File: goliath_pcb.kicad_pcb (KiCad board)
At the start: 2 copper layers, 138.4 x 81.9 mm, 56 parts, among them IC1 MCT9001SD, IC2 MCT9001SD, IC3 MCT9001SD, IC4 MCT9001SD, IC5 MCT9001SD, IC6 MCT9001SD, IC7 MCT9001SD, J1 RJ45_LED, J2 RJ45_LED, J3 RJ45_LED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

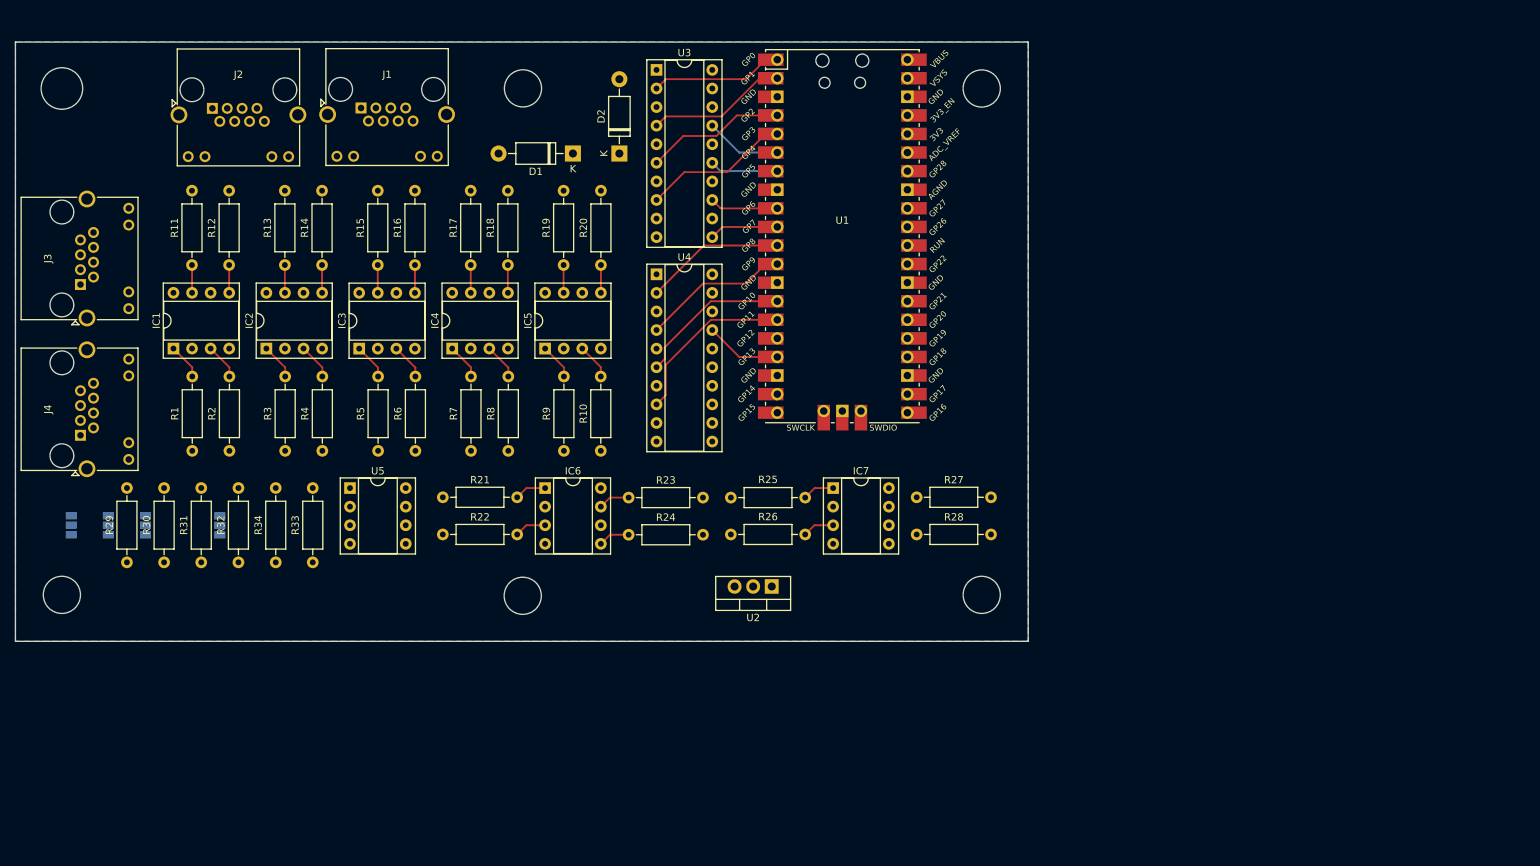
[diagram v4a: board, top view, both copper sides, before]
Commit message: Add xBee initial plan
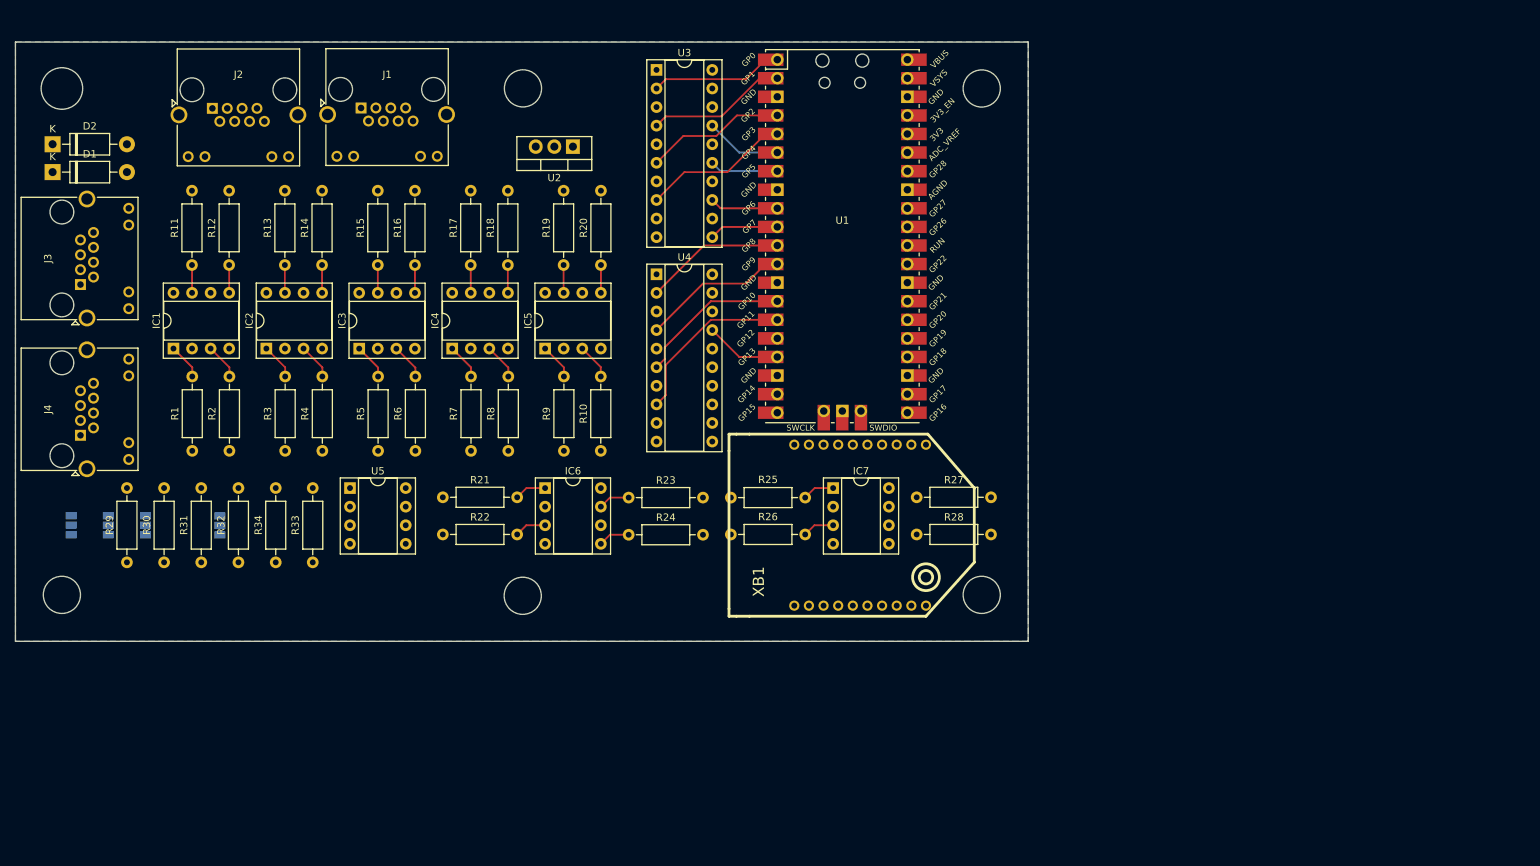
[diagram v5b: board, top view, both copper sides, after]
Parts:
- added XB1: XBEE, RF_and_other_modules:XBEE_PRO_PTH, F.Cu at (160.0, 113.0)
- moved D2 77.5 mm to (40.6, 61.0), turned to 0 degrees
- moved D1 71.2 mm to (40.6, 64.8), turned to 0 degrees
- moved U2 66.0 mm to (111.8, 61.3)
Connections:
- U1 pad 21: Net-(J4-Pad3) -> Net-(U1-Pad21)
- U1 pad 22: Net-(J4-Pad4) -> Net-(U1-Pad22)
- U1 pad 24: unconnected-(U1-Pad24) -> Net-(J4-Pad3)
- U1 pad 25: unconnected-(U1-Pad25) -> Net-(J4-Pad4)

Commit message: Run traces for current version
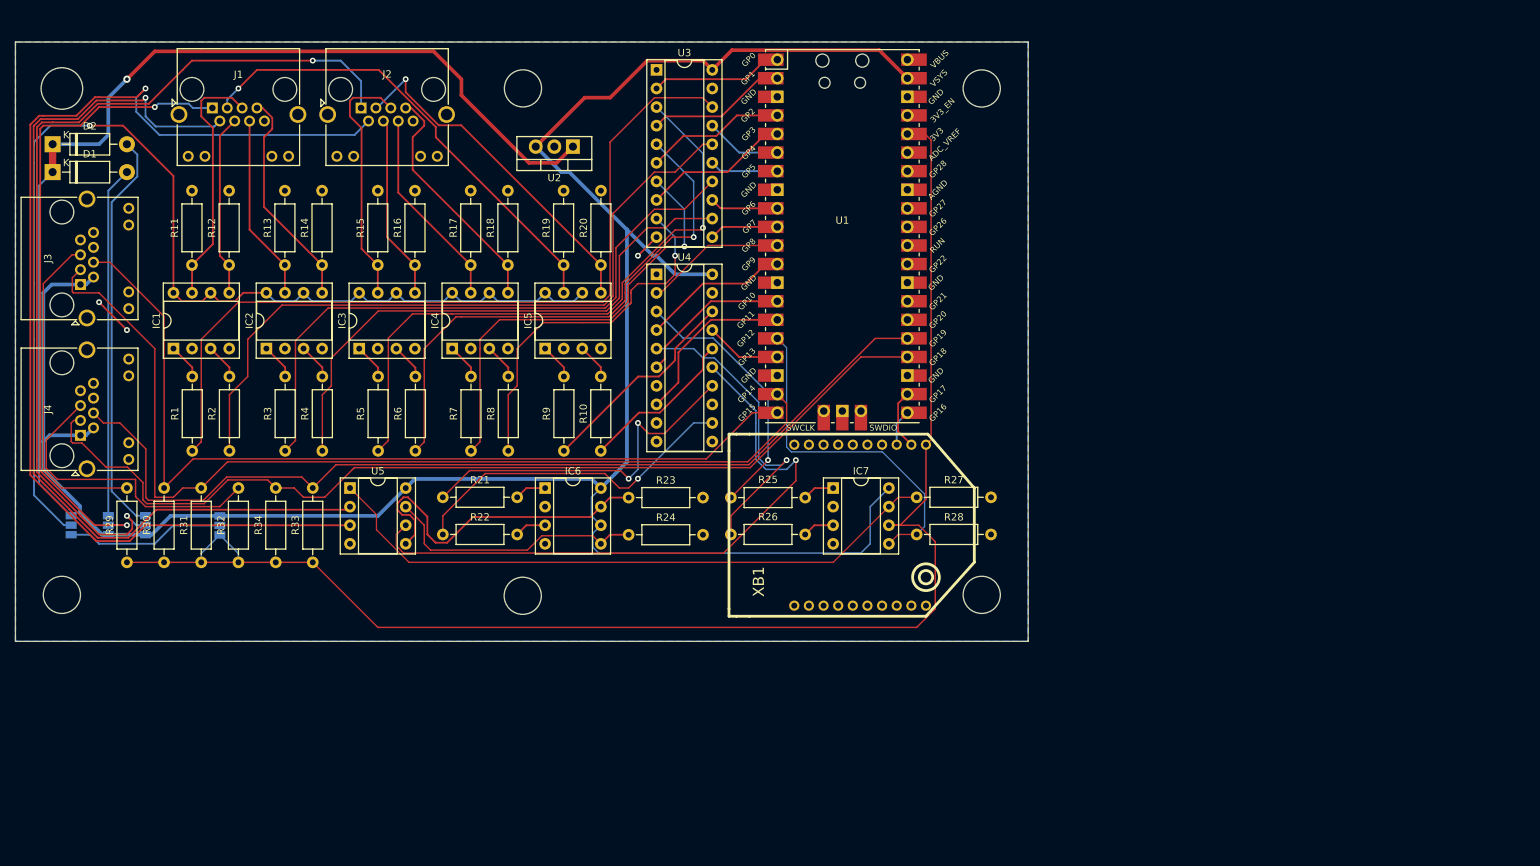
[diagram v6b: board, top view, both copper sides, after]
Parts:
- moved J2 20.3 mm to (82.8, 56.0)
- moved J1 20.3 mm to (62.5, 56.0)
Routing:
- net 5V: track 0.00 -> 307.7 mm
- net 3.3V: track 0.00 -> 200.8 mm
- net LGV: track 0.00 -> 158.1 mm, vias 0 -> 1
- net Net-(J2-Pad2): track 0.00 -> 151.6 mm, vias 0 -> 1
- net 12V: track 0.00 -> 141.2 mm, vias 0 -> 1
- net Net-(J4-Pad3): track 0.00 -> 133.4 mm
- net Net-(J3-Pad3): track 0.00 -> 133.3 mm
- net Net-(J4-Pad4): track 0.00 -> 130.5 mm
- net Net-(J1-Pad2): track 0.00 -> 126.6 mm, vias 0 -> 1
- net Net-(J3-Pad4): track 0.00 -> 124.3 mm
- net Net-(J2-Pad1): track 0.00 -> 122.1 mm, vias 0 -> 2
- net Net-(R1-Pad1): track 0.00 -> 112.0 mm
- net Net-(R2-Pad1): track 0.00 -> 97.4 mm
- net Net-(J1-Pad1): track 0.00 -> 89.4 mm, vias 0 -> 2
- net Net-(U4-Pad15): track 0.00 -> 86.9 mm, vias 0 -> 1
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
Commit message: Add extra I/O and extra headers, expand PCB
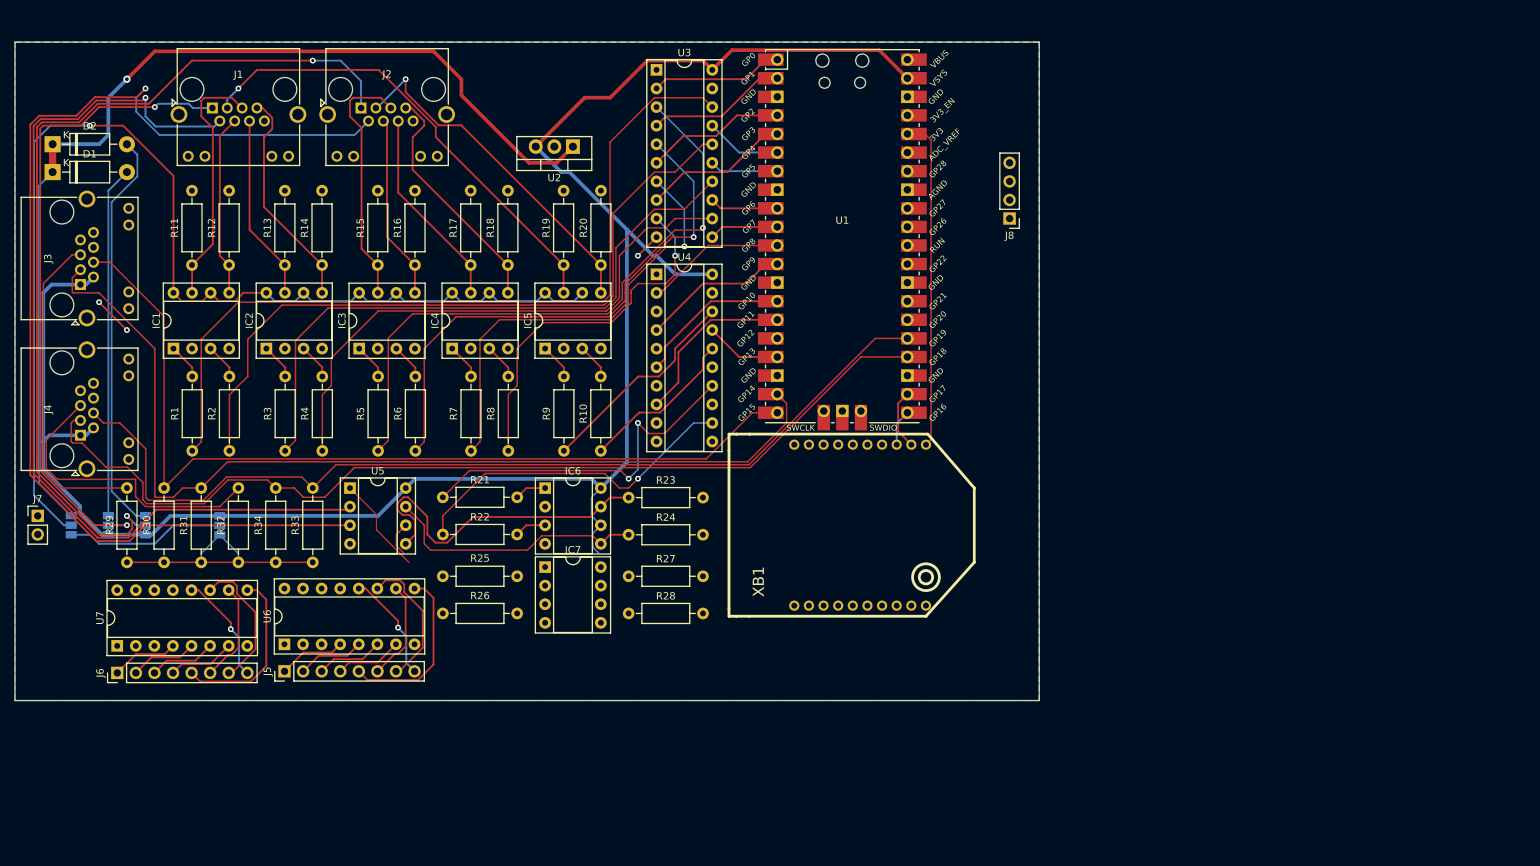
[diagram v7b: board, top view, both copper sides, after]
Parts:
- added J5: Conn_01x08_Male, Connector_PinHeader_2.54mm:PinHeader_1x08_P2.54mm_Vertical, F.Cu at (72.3, 133.0)
- added J6: Conn_01x08_Male, Connector_PinHeader_2.54mm:PinHeader_1x08_P2.54mm_Vertical, F.Cu at (49.5, 133.2)
- added J7: Conn_01x02_Male, Connector_PinHeader_2.54mm:PinHeader_1x02_P2.54mm_Vertical, F.Cu at (38.6, 111.8)
- added J8: Conn_01x04_Male, Connector_PinHeader_2.54mm:PinHeader_1x04_P2.54mm_Vertical, F.Cu at (171.4, 71.1)
- added U6: PCF8574, Package_DIP:DIP-16_W7.62mm_Socket, F.Cu at (72.3, 129.3)
- added U7: PCF8574, Package_DIP:DIP-16_W7.62mm_Socket, F.Cu at (49.5, 129.5)
- moved IC7 40.8 mm to (108.0, 118.8)
- moved R27 40.8 mm to (119.4, 120.0)
- moved R28 40.8 mm to (119.4, 125.1)
- moved R26 40.8 mm to (94.0, 125.1)
- moved R25 40.8 mm to (104.1, 120.0)
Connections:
- U1 pad 16: Net-(IC7-Pad5) -> Net-(U1-Pad16)
- U1 pad 17: Net-(U1-Pad17) -> Net-(IC7-Pad5)
- U1 pad 26: unconnected-(U1-Pad26) -> Net-(U1-Pad26)
- U1 pad 27: unconnected-(U1-Pad27) -> Net-(U1-Pad27)
- U1 pad 29: unconnected-(U1-Pad29) -> Net-(J8-Pad1)
- U1 pad 31: unconnected-(U1-Pad31) -> Net-(J8-Pad2)
- U1 pad 32: unconnected-(U1-Pad32) -> Net-(J8-Pad3)
- U1 pad 34: unconnected-(U1-Pad34) -> Net-(J8-Pad4)
- U4 pad 17: Net-(U1-Pad17) -> Net-(U1-Pad16)
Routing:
- net 3.3V: track 200.8 -> 80.5 mm
- net Net-(U4-Pad15): track 86.9 -> 4.74 mm, vias 1 -> 0
- net Net-(IC7-Pad7): track 86.6 -> 13.5 mm
- net 5V: track 307.7 -> 261.4 mm
- net Net-(R26-Pad1): track 42.5 -> 0.00 mm, vias 1 -> 0
- net Net-(IC7-Pad5): track 47.2 -> 10.4 mm
- net Net-(R25-Pad2): track 36.3 -> 0.00 mm, vias 1 -> 0
- net Net-(J5-Pad5): track 0.00 -> 23.8 mm
- net Net-(J6-Pad5): track 0.00 -> 23.8 mm
- net Net-(J5-Pad7): track 0.00 -> 19.1 mm
- net Net-(J6-Pad7): track 0.00 -> 19.1 mm
- net Net-(J6-Pad8): track 0.00 -> 15.0 mm, vias 0 -> 1
- net Net-(J5-Pad8): track 0.00 -> 15.0 mm, vias 0 -> 1
- net Net-(J6-Pad6): track 0.00 -> 13.7 mm
- net Net-(J5-Pad6): track 0.00 -> 13.7 mm
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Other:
- board size 138.4 x 81.9 mm -> 140 x 90 mm

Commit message: Add more resistors, caps
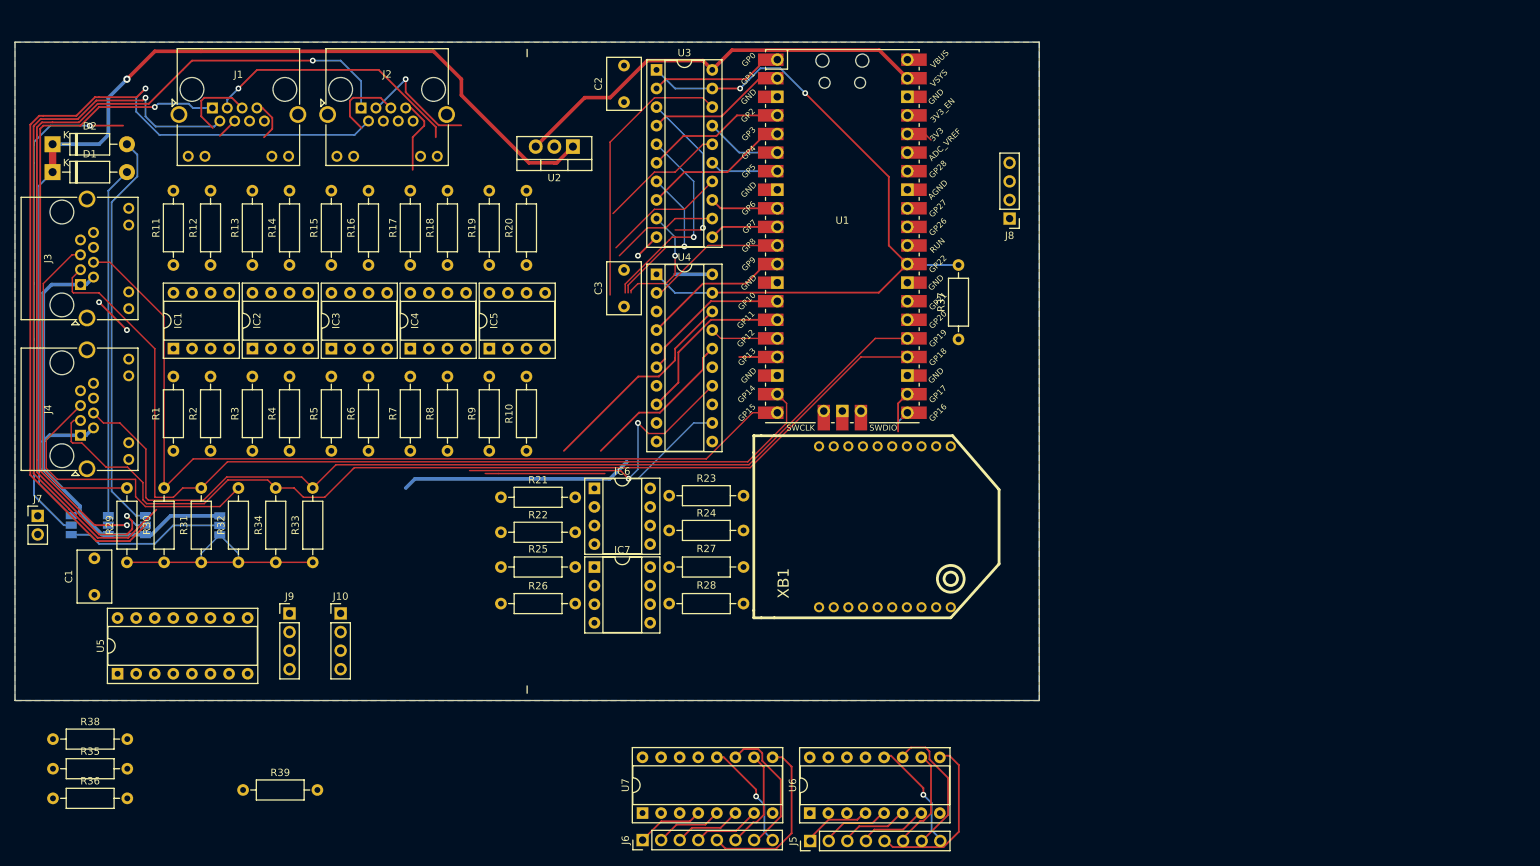
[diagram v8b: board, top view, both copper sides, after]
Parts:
- added C1: 1uF, Capacitor_THT:C_Rect_L7.0mm_W4.5mm_P5.00mm, F.Cu at (46.4, 122.6)
- added C2: 1uF, Capacitor_THT:C_Rect_L7.0mm_W4.5mm_P5.00mm, F.Cu at (118.7, 55.2)
- added C3: 1uF, Capacitor_THT:C_Rect_L7.0mm_W4.5mm_P5.00mm, F.Cu at (118.7, 83.1)
- added J10: Conn_01x04_Male, Connector_PinHeader_2.54mm:PinHeader_1x04_P2.54mm_Vertical, F.Cu at (80.0, 125.1)
- added J9: Conn_01x04_Male, Connector_PinHeader_2.54mm:PinHeader_1x04_P2.54mm_Vertical, F.Cu at (73.0, 125.1)
- added R35: 10k, Resistor_THT:R_Axial_DIN0207_L6.3mm_D2.5mm_P10.16mm_Horizontal, F.Cu at (40.7, 146.3)
- added R36: 10k, Resistor_THT:R_Axial_DIN0207_L6.3mm_D2.5mm_P10.16mm_Horizontal, F.Cu at (40.7, 150.4)
- added R37: 10k, Resistor_THT:R_Axial_DIN0207_L6.3mm_D2.5mm_P10.16mm_Horizontal, F.Cu at (164.5, 87.6)
- added R38: 10k, Resistor_THT:R_Axial_DIN0207_L6.3mm_D2.5mm_P10.16mm_Horizontal, F.Cu at (40.7, 142.3)
- added R39: 10k, Resistor_THT:R_Axial_DIN0207_L6.3mm_D2.5mm_P10.16mm_Horizontal, F.Cu at (66.7, 149.2)
- U5: value LTC1298CS8-PBF -> MCP3008; footprint Package_DIP:DIP-8_W7.62mm_Socket -> Package_DIP:DIP-16_W7.62mm_Socket
- moved J5 75.5 mm to (144.2, 156.2)
- moved U6 75.4 mm to (144.1, 152.4)
- moved U7 75.4 mm to (121.3, 152.4)
- moved J6 75.4 mm to (121.3, 156.1)
- moved U5 40.7 mm to (49.5, 133.3), turned to 90 degrees
- moved R9 10.2 mm to (100.3, 102.9)
- moved R20 10.2 mm to (105.4, 77.5)
- moved R10 10.2 mm to (105.4, 102.9)
- moved R19 10.2 mm to (100.3, 77.5)
- moved R8 8.32 mm to (94.6, 102.9)
- moved R7 8.30 mm to (89.5, 102.9)
- moved R17 8.26 mm to (89.5, 77.5)
- moved R18 8.26 mm to (94.6, 77.5)
- moved R26 8.05 mm to (101.9, 123.8)
- moved R25 8.04 mm to (112.1, 118.8)
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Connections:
- J8 pad 1: Net-(J8-Pad1) -> unconnected-(J8-Pad1)
- U1 pad 16: Net-(U1-Pad16) -> Net-(IC7-Pad5)
- U1 pad 17: Net-(IC7-Pad5) -> Net-(U1-Pad17)
- U1 pad 29: Net-(J8-Pad1) -> Net-(R37-Pad2)
- U3 pad 1: GND -> Net-(R37-Pad2)
- U3 pad 19: GND -> Net-(R37-Pad2)
- U4 pad 1: GND -> Net-(R37-Pad2)
- U4 pad 11: unconnected-(U4-Pad11) -> GND
- U4 pad 13: unconnected-(U4-Pad13) -> GND
- U4 pad 17: Net-(U1-Pad16) -> Net-(U1-Pad17)
- U4 pad 19: GND -> Net-(R37-Pad2)
- U5 pad 1: Net-(IC7-Pad7) -> Net-(J1-Pad2)
- U5 pad 2: Net-(J1-Pad2) -> Net-(J2-Pad2)
- U5 pad 3: Net-(J2-Pad2) -> Net-(U5-Pad3)
- U5 pad 4: GND -> Net-(U5-Pad4)
- U5 pad 5: Net-(IC6-Pad7) -> unconnected-(U5-Pad5)
- U5 pad 6: Net-(U4-Pad15) -> unconnected-(U5-Pad6)
- U5 pad 7: Net-(IC6-Pad5) -> unconnected-(U5-Pad7)
- U5 pad 8: 5V -> unconnected-(U5-Pad8)
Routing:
- net Net-(R37-Pad2): track 0.00 -> 97.1 mm, vias 0 -> 2
- net 5V: track 261.4 -> 164.6 mm
- net LGV: track 158.1 -> 68.2 mm
- net Net-(R2-Pad1): track 97.4 -> 17.5 mm
- net Net-(R1-Pad1): track 112.0 -> 37.9 mm
- net Net-(R3-Pad1): track 85.6 -> 16.9 mm
- net Net-(R5-Pad1): track 85.7 -> 23.1 mm
- net Net-(R4-Pad1): track 76.6 -> 14.8 mm
- net Net-(J5-Pad6): track 13.7 -> 71.6 mm, vias 0 -> 1
- net Net-(IC6-Pad7): track 46.1 -> 0.00 mm
- net Net-(R6-Pad1): track 73.7 -> 28.0 mm
- net 3.3V: track 80.5 -> 38.6 mm
- net Net-(R7-Pad1): track 60.7 -> 21.4 mm
- net Net-(IC6-Pad5): track 36.2 -> 0.00 mm
- net Net-(R8-Pad1): track 49.9 -> 15.9 mm
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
